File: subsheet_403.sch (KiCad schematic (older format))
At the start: 44 parts, among them Q404 2N3904, Q405 2N3904, U403 MC1377_COLOR_TELEVISION_RGB_T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

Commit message: Delete circuitry related to PAL/NTSC and modulator
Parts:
- removed C415: 470uF, commons_passives_THT:Passive_THT_capacitor_polarized_rad_D10.16mm_P5.08mm_H22.86mm, symbol Device:CP1
- removed C417, C423: 100uF, commons_passives_THT:Passive_THT_capacitor_polarized_rad_D5.08mm_P2.54mm_H12.70mm, symbol Device:CP1
- removed C418: 2200pF, commons_passives_THT:Passive_THT_capacitor_W2.54mm_L10.16mm, symbol Device:C
- removed C419, C422, C428, C429: 0.1uF, commons_passives_THT:Passive_THT_capacitor_mlcc_W2.54mm_L7.62mm, symbol Device:C
- removed C420, C424, C426: 15uF, Capacitor_THT:CP_Radial_Tantal_D4.5mm_P2.50mm, symbol Device:CP1
- removed C421: 120pF, commons_passives_THT:Passive_THT_capacitor_W2.54mm_L10.16mm, symbol Device:C
- removed C425: 2200pF, commons_passives_THT:Passive_THT_capacitor_polarized_rad_D5.08mm_P2.54mm_H12.70mm, symbol Device:C
- removed C427: 0.001uF, commons_passives_THT:Passive_THT_capacitor_W2.54mm_L10.16mm, symbol Device:C
- removed C430, C431: 0.01uF, commons_passives_THT:Passive_THT_capacitor_W2.54mm_L10.16mm, symbol Device:C
- removed C432: 0.001uF, commons_passives_THT:Passive_THT_capacitor_ceramic_radial_W2.54mm_L10.16mm, symbol Device:C
- removed C433: 1uF, commons_passives_THT:Passive_THT_capacitor_polarized_rad_D5.08mm_P2.54mm_H12.70mm, symbol Device:CP1
- removed DL1: Delay Line 3.58MHz, atari-passives_THT:Atari_ST_THT_Delay_Line, symbol Delay_Line_Custom_Atari_ST:Delay_Line_Custom_Atari_ST
- removed L403: Var. coil 24uH, commons_passives_THT:Passive_THT_variable_Coil_Shielded_7x7mm_5_of_6pins, symbol variable_coil_shielded:Variable_Coil_Shielded
- removed MOD1: ST Modulator, Connector_PinHeader_2.54mm:PinHeader_1x03_P2.54mm_Vertical, symbol Connector_Generic_Shielded:Conn_01x03_Shielded
- removed Q404: 2N3904, Package_TO_SOT_THT:TO-92_Inline_Wide, symbol Transistor_BJT:2N3904
- removed R405, R451, R459: 0, commons_passives_THT:Passive_THT_resistor_W2.54mm_L12.70mm, symbol Device:R_Small_US
- removed R439: 75, commons_passives_THT:Passive_THT_resistor_W2.54mm_L12.70mm, symbol Device:R_Small_US
- removed R442, R463, R470: 1K, commons_passives_THT:Passive_THT_resistor_W2.54mm_L12.70mm, symbol Device:R_Small_US
- removed R448: 150, commons_passives_THT:Passive_THT_resistor_W2.54mm_L12.70mm, symbol Device:R_Small_US
- removed R452: 1K5, commons_passives_THT:Passive_THT_resistor_W2.54mm_L12.70mm, symbol Device:R_Small_US
- removed R456: 2K2, commons_passives_THT:Passive_THT_resistor_W2.54mm_L12.70mm, symbol Device:R_Small_US
- removed R467, R468: 1K2, commons_passives_THT:Passive_THT_resistor_W2.54mm_L12.70mm, symbol Device:R_Small_US
- removed R469: 5K6, commons_passives_THT:Passive_THT_resistor_W2.54mm_L12.70mm, symbol Device:R_Small_US
- removed R471: 47K, commons_passives_THT:Passive_THT_resistor_W2.54mm_L12.70mm, symbol Device:R_Small_US
- removed U403: MC1377_COLOR_TELEVISION_RGB_TO_PAL_NTSC_ENCODER_P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, Package_DIP:DIP-20_W7.62mm_LongPads, symbol mc1377:MC1377_COLOR_TELEVISION_RGB_TO_PAL_NTSC_ENCODER_PHY
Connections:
- net labels removed: +12V, AUDIO, B, CCLK, G, NOT__HSYNC_XOR_VSYNC, R, SHIFTER_COLOR, b_y_clamp, blue, chroma_in, chroma_out, cv_out, decoupler, green, ntsc_select, osc_in, r_y_clamp, red, tr, v_clamp, volt_bias, y_in, y_out
- wire segments 130 -> 19
- no-connect marks 6 -> 0
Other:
- note removed: "About L403 and DL1 : I made custom symbols to match the pins written on the schematics.\n\nFor DL1 : \n\nI compared with the schematics of the Atari MegaSTe rev C and of the Falcon030. Pin 12 appears grounded on the former ; on the later, pin 9, 10 and 12 appears grounded, \nwith pin 10 taking the central position, while pin 3 and 6 are bridged together. \n\nIn the gerber of the sparrow (found as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"
- note removed: "C415 should be the other way around. On the ST schematics\nthis is C21, the cathode (-) is connected to the resistor\nthat outputs CSYNC/Composite.\n\nsee https://www.exxoshost.co.uk/forum/viewtopic.php?f=17&t=1698"
- note removed: "Change values for PAL (I took them from the Falcon030 service manual\nafter checking that this part of the schematics is the same as the\nSTe - lucky me)\n\n* C421 : 100pF\n* DL1 : 4.43MHz\n* L403 : 14uH\n* R451 : 22\n* R456 : 1K8 (PAL-I) ; 2K7 (PAL-B)\n* R463 : 1K2\n\nDid you know there was several PAL variant ? \n* PAL-I is for UK/Ireland\n* PAL-B is for Western Europe, Australia and New Zealand"
- note removed: "Installed ONLY in systems with modulator"
- note removed: "NTSC clock"
- note removed: "PAL carrier clock"
- note removed: "Remove\nfor PAL"
- note removed: "bridged on my \nmotherboard"
- note removed: "maybe grounded"

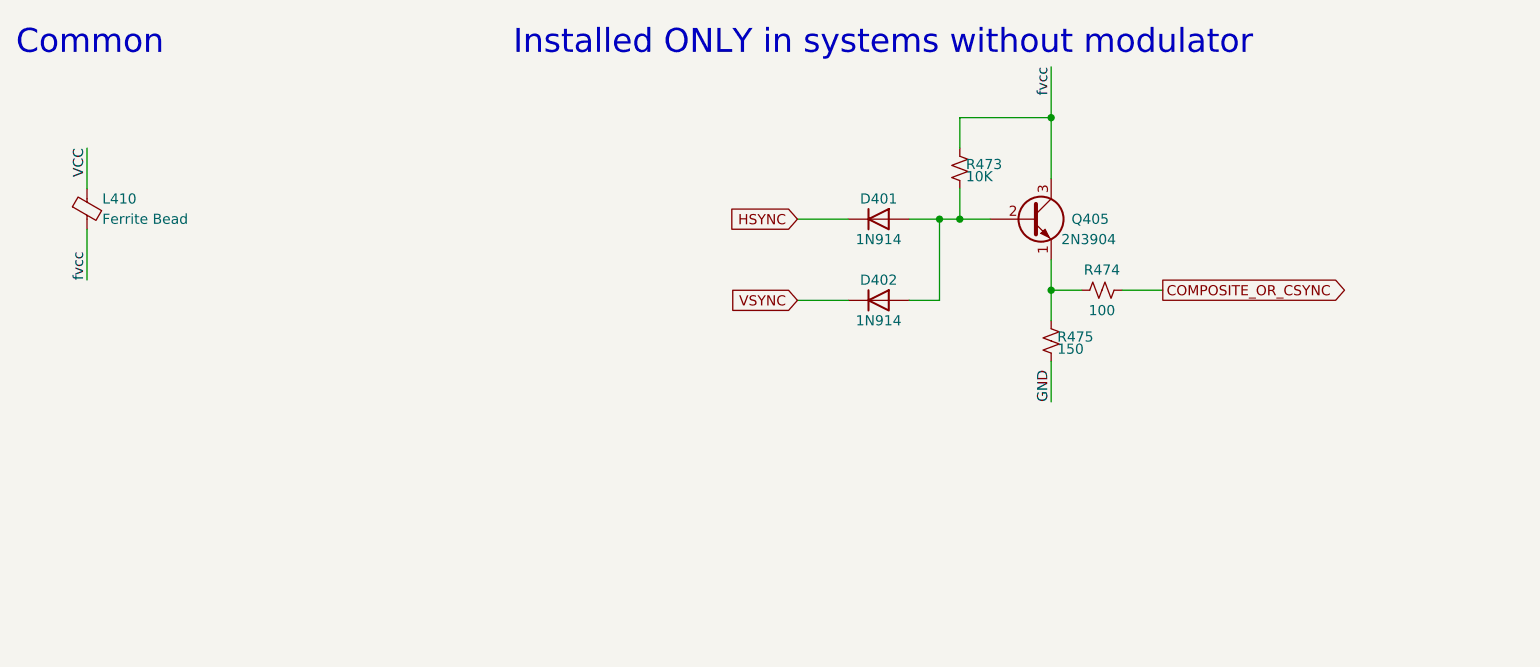
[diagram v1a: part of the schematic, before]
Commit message: Resolves #1 : Use 4-resistor packs wherever it is possible
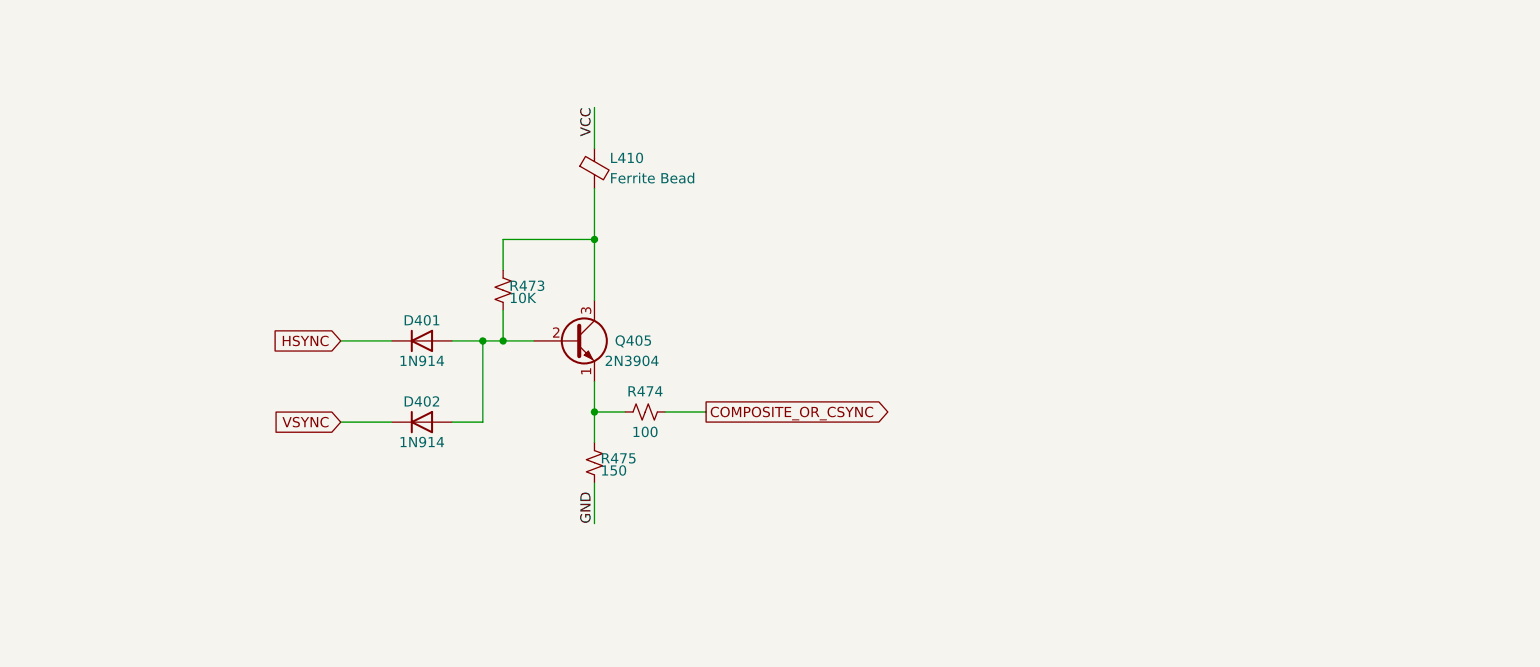
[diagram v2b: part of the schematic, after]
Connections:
- net fvcc: no longer names the net of L410.2, Q405.3 (C), R473.1
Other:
- note removed: "Common"
- note removed: "Installed ONLY in systems without modulator"
- moved on the sheet: D401, D402, L410, Q405, R473, R474, R475
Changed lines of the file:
@@
 L Device:Ferrite_Bead_Small L?
 U 1 1 60C12DAA
-P 1500 1500
+P 4000 1300
 AR Path="/60B3D9E3/60C12DAA" Ref="L?"  Part="1"
 AR Path="/60B8B7AD/60C12DAA" Ref="L410"  Part="1"
-F 0 "L410" H 1575 1550 50  0000 L CNN
-F 1 "Ferrite Bead" H 1575 1450 50  0000 L CNN
-F 2 "commons_passives_THT:Passive_THT_ferrite_bead_W3.81mm_L15.24mm" V 1430 1500 50  0001 C CNN
-F 3 "~" H 1500 1500 50  0001 C CNN
-	1    1500 1500
+F 0 "L410" H 4075 1350 50  0000 L CNN
+F 1 "Ferrite Bead" H 4075 1250 50  0000 L CNN
+F 2 "commons_passives_THT:Passive_THT_ferrite_bead_W3.81mm_L15.24mm" V 3930 1300 50  0001 C CNN
+F 3 "~" H 4000 1300 50  0001 C CNN
+	1    4000 1300
 	1    0    0    -1
 $EndComp
 Wire Wire Line
-	1500 1400 1500 1200
-Text Label 1500 1200 3    50   ~ 0
+	4000 1200 4000 1000
+Text Label 4000 1000 3    50   ~ 0
 VCC
-Text Label 1500 1850 1    50   ~ 0
-fvcc
 Wire Wire Line
-	1500 1850 1500 1600
-Text Notes 3600 750  0    118  ~ 0
-Installed ONLY in systems without modulator
+	4000 1650 4000 1400
 $Comp
 L Transistor_BJT:2N3904 Q?
 U 1 1 60C878BF
-P 6150 1550
+P 3900 2150
 AR Path="/60B3D9E3/60C878BF" Ref="Q?"  Part="1"
 AR Path="/60B8B7AD/60C878BF" Ref="Q405"  Part="1"
-F 0 "Q405" H 6350 1550 50  0000 L CNN
-F 1 "2N3904" H 6300 1450 50  0000 L CNN
-F 2 "Package_TO_SOT_THT:TO-92_Inline_Wide" H 6350 1475 50  0001 L CIN
-F 3 "https://www.onsemi.com/pub/Collateral/2N3903-D.PDF" H 6150 1550 50  0001 L CNN
-	1    6150 1550
+F 0 "Q405" H 4100 2150 50  0000 L CNN
+F 1 "2N3904" H 4050 2050 50  0000 L CNN
+F 2 "Package_TO_SOT_THT:TO-92_Inline_Wide" H 4100 2075 50  0001 L CIN
+F 3 "https://www.onsemi.com/pub/Collateral/2N3903-D.PDF" H 3900 2150 50  0001 L CNN
+	1    3900 2150
 	1    0    0    -1
 $EndComp
@@
 L Device:R_Small_US R?
 U 1 1 60C887E0
-P 5800 1300
+P 3550 1900
 AR Path="/60B3D9E3/60C887E0" Ref="R?"  Part="1"
 AR Path="/60B8B7AD/60C887E0" Ref="R473"  Part="1"
-F 0 "R473" H 5830 1320 50  0000 L CNN
-F 1 "10K" H 5830 1260 50  0000 L CNN
-F 2 "commons_passives_THT:Passive_THT_resistor_W2.54mm_L12.70mm" H 5800 1300 50  0001 C CNN
-F 3 "~" H 5800 1300 50  0001 C CNN
-	1    5800 1300
+F 0 "R473" H 3580 1920 50  0000 L CNN
+F 1 "10K" H 3580 1860 50  0000 L CNN
+F 2 "commons_passives_THT:Passive_THT_resistor_W2.54mm_L12.70mm" H 3550 1900 50  0001 C CNN
+F 3 "~" H 3550 1900 50  0001 C CNN
+	1    3550 1900
 	1    0    0    -1
 $EndComp
@@
 L Device:R_Small_US R?
 U 1 1 60C8E2E8
-P 6250 2150
+P 4000 2750
 AR Path="/60B3D9E3/60C8E2E8" Ref="R?"  Part="1"
 AR Path="/60B8B7AD/60C8E2E8" Ref="R475"  Part="1"
-F 0 "R475" H 6280 2170 50  0000 L CNN
-F 1 "150" H 6280 2110 50  0000 L CNN
-F 2 "commons_passives_THT:Passive_THT_resistor_W2.54mm_L12.70mm" H 6250 2150 50  0001 C CNN
-F 3 "~" H 6250 2150 50  0001 C CNN
-	1    6250 2150
+F 0 "R475" H 4030 2770 50  0000 L CNN
+F 1 "150" H 4030 2710 50  0000 L CNN
+F 2 "commons_passives_THT:Passive_THT_resistor_W2.54mm_L12.70mm" H 4000 2750 50  0001 C CNN
+F 3 "~" H 4000 2750 50  0001 C CNN
+	1    4000 2750
 	1    0    0    -1
 $EndComp
-Text Label 6250 2450 1    50   ~ 0
+Text Label 4000 3050 1    50   ~ 0
 GND
 Wire Wire Line
-	6250 2250 6250 2450
+	4000 2850 4000 3050
 $Comp
 L Device:R_Small_US R?
 U 1 1 60C9CC6E
-P 6500 1900
+P 4250 2500
 AR Path="/608A2359/60C9CC6E" Ref="R?"  Part="1"
 AR Path="/60A1445F/60C9CC6E" Ref="R?"  Part="1"
@@
 AR Path="/60B3D9E3/60C9CC6E" Ref="R?"  Part="1"
 AR Path="/60B8B7AD/60C9CC6E" Ref="R474"  Part="1"
-F 0 "R474" V 6400 1900 50  0000 C CNN
-F 1 "100" V 6600 1900 50  0000 C CNN
-F 2 "commons_passives_THT:Passive_THT_resistor_W2.54mm_L12.70mm" H 6500 1900 50  0001 C CNN
-F 3 "~" H 6500 1900 50  0001 C CNN
-	1    6500 1900
+F 0 "R474" V 4150 2500 50  0000 C CNN
+F 1 "100" V 4350 2500 50  0000 C CNN
+F 2 "commons_passives_THT:Passive_THT_resistor_W2.54mm_L12.70mm" H 4250 2500 50  0001 C CNN
+F 3 "~" H 4250 2500 50  0001 C CNN
+	1    4250 2500
 	0    1    1    0
 $EndComp
@@
 L Device:D D401
 U 1 1 60CA07DA
-P 5400 1550
-F 0 "D401" H 5400 1650 50  0000 C CNN
-F 1 "1N914" H 5400 1450 50  0000 C CNN
-F 2 "commons_passives_THT:Passive_THT_diode_W2.54mm_L12.70mm" H 5400 1550 50  0001 C CNN
-F 3 "~" H 5400 1550 50  0001 C CNN
-	1    5400 1550
+P 3150 2150
+F 0 "D401" H 3150 2250 50  0000 C CNN
+F 1 "1N914" H 3150 2050 50  0000 C CNN
+F 2 "commons_passives_THT:Passive_THT_diode_W2.54mm_L12.70mm" H 3150 2150 50  0001 C CNN
+F 3 "~" H 3150 2150 50  0001 C CNN
+	1    3150 2150
 	1    0    0    -1
 $EndComp
@@
 L Device:D D402
 U 1 1 60CA1114
-P 5400 1950
-F 0 "D402" H 5400 2050 50  0000 C CNN
-F 1 "1N914" H 5400 1850 50  0000 C CNN
-F 2 "commons_passives_THT:Passive_THT_diode_W2.54mm_L12.70mm" H 5400 1950 50  0001 C CNN
-F 3 "~" H 5400 1950 50  0001 C CNN
-	1    5400 1950
+P 3150 2550
+F 0 "D402" H 3150 2650 50  0000 C CNN
+F 1 "1N914" H 3150 2450 50  0000 C CNN
+F 2 "commons_passives_THT:Passive_THT_diode_W2.54mm_L12.70mm" H 3150 2550 50  0001 C CNN
+F 3 "~" H 3150 2550 50  0001 C CNN
+	1    3150 2550
 	1    0    0    -1
 $EndComp
-Text Label 6250 800  3    50   ~ 0
-fvcc
 Wire Wire Line
-	6250 800  6250 1050
+	4000 1650 3550 1650
 Wire Wire Line
-	6250 1050 5800 1050
+	3550 1650 3550 1800
+Connection ~ 4000 1650
 Wire Wire Line
-	5800 1050 5800 1200
-Connection ~ 6250 1050
+	4000 1650 4000 1950
 Wire Wire Line
-	6250 1050 6250 1350
+	3550 2000 3550 2150
 Wire Wire Line
-	5800 1400 5800 1550
+	3550 2150 3700 2150
 Wire Wire Line
-	5800 1550 5950 1550
+	3300 2150 3450 2150
+Connection ~ 3550 2150
 Wire Wire Line
-	5550 1550 5700 1550
-Connection ~ 5800 1550
+	3300 2550 3450 2550
 Wire Wire Line
-	5550 1950 5700 1950
+	3450 2550 3450 2150
+Connection ~ 3450 2150
 Wire Wire Line
-	5700 1950 5700 1550
-Connection ~ 5700 1550
+	3450 2150 3550 2150
 Wire Wire Line
-	5700 1550 5800 1550
+	4000 2350 4000 2500
 Wire Wire Line
-	6250 1750 6250 1900
+	4000 2500 4150 2500
+Connection ~ 4000 2500
 Wire Wire Line
-	6250 1900 6400 1900
-Connection ~ 6250 1900
-Wire Wire Line
-	6250 1900 6250 2050
-Text GLabel 6800 1900 2    50   Output ~ 0
+	4000 2500 4000 2650
+Text GLabel 4550 2500 2    50   Output ~ 0
 COMPOSITE_OR_CSYNC
 Wire Wire Line
-	6600 1900 6800 1900
-Text GLabel 5000 1550 0    50   Input ~ 0
+	4350 2500 4550 2500
+Text GLabel 2750 2150 0    50   Input ~ 0
 HSYNC
-Text GLabel 5000 1950 0    50   Input ~ 0
+Text GLabel 2750 2550 0    50   Input ~ 0
 VSYNC
 Wire Wire Line
-	5000 1550 5250 1550
+	2750 2150 3000 2150
 Wire Wire Line
-	5000 1950 5250 1950
-Text Notes 1150 750  0    118  ~ 0
-Common
+	2750 2550 3000 2550
 Wire Notes Line
 	7800 5900 7800 5400

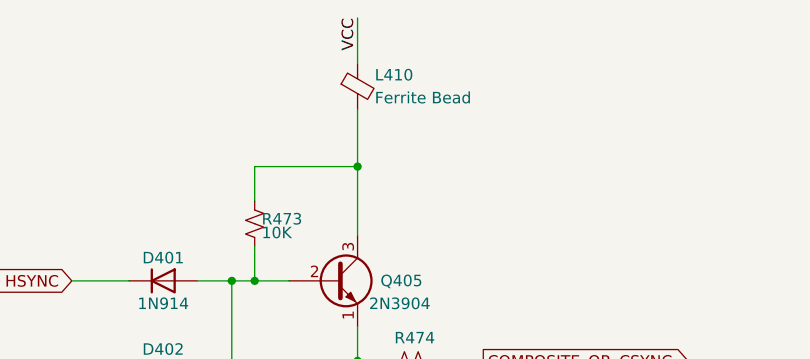
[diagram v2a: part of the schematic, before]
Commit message: Resolves #11 : Use the reference 'FB?' for the ferrite beads
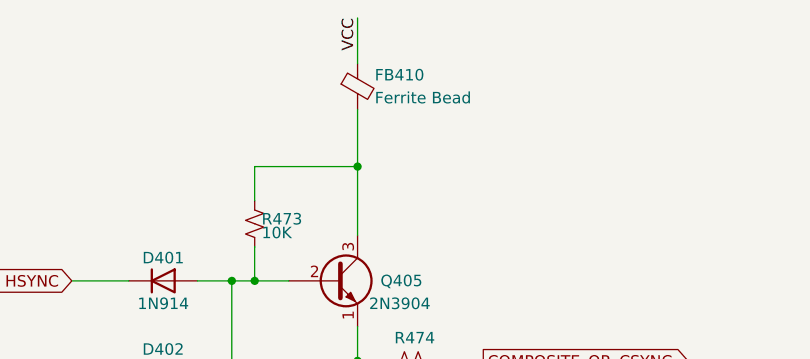
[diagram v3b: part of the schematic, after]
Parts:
- renumbered L410 to FB410
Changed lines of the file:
@@
 P 4000 1300
 AR Path="/60B3D9E3/60C12DAA" Ref="L?"  Part="1"
-AR Path="/60B8B7AD/60C12DAA" Ref="L410"  Part="1"
-F 0 "L410" H 4075 1350 50  0000 L CNN
+AR Path="/60B8B7AD/60C12DAA" Ref="FB410"  Part="1"
+F 0 "FB410" H 4075 1350 50  0000 L CNN
 F 1 "Ferrite Bead" H 4075 1250 50  0000 L CNN
 F 2 "commons_passives_THT:Passive_THT_ferrite_bead_W3.81mm_L15.24mm" V 3930 1300 50  0001 C CNN

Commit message: Resolves #13 : assign 1206 hand-solder footprints to resistors
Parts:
- R473, R474, R475: footprint commons_passives_THT:Passive_THT_resistor_W2.54mm_L12.70mm -> Resistor_SMD:R_1206_3216Metric_Pad1.30x1.75mm_HandSolder
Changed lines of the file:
@@
 F 0 "R473" H 3580 1920 50  0000 L CNN
 F 1 "10K" H 3580 1860 50  0000 L CNN
-F 2 "commons_passives_THT:Passive_THT_resistor_W2.54mm_L12.70mm" H 3550 1900 50  0001 C CNN
+F 2 "Resistor_SMD:R_1206_3216Metric_Pad1.30x1.75mm_HandSolder" H 3550 1900 50  0001 C CNN
 F 3 "~" H 3550 1900 50  0001 C CNN
 	1    3550 1900
@@
 F 0 "R475" H 4030 2770 50  0000 L CNN
 F 1 "150" H 4030 2710 50  0000 L CNN
-F 2 "commons_passives_THT:Passive_THT_resistor_W2.54mm_L12.70mm" H 4000 2750 50  0001 C CNN
+F 2 "Resistor_SMD:R_1206_3216Metric_Pad1.30x1.75mm_HandSolder" H 4000 2750 50  0001 C CNN
 F 3 "~" H 4000 2750 50  0001 C CNN
 	1    4000 2750
@@
 F 0 "R474" V 4150 2500 50  0000 C CNN
 F 1 "100" V 4350 2500 50  0000 C CNN
-F 2 "commons_passives_THT:Passive_THT_resistor_W2.54mm_L12.70mm" H 4250 2500 50  0001 C CNN
+F 2 "Resistor_SMD:R_1206_3216Metric_Pad1.30x1.75mm_HandSolder" H 4250 2500 50  0001 C CNN
 F 3 "~" H 4250 2500 50  0001 C CNN
 	1    4250 2500

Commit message: Resolves #14 : assign smd footprints for ferrite beads
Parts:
- FB410: footprint commons_passives_THT:Passive_THT_ferrite_bead_W3.81mm_L15.24mm -> Inductor_SMD:L_1206_3216Metric_Pad1.22x1.90mm_HandSolder
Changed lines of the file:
@@
 F 0 "FB410" H 4075 1350 50  0000 L CNN
 F 1 "Ferrite Bead" H 4075 1250 50  0000 L CNN
-F 2 "commons_passives_THT:Passive_THT_ferrite_bead_W3.81mm_L15.24mm" V 3930 1300 50  0001 C CNN
+F 2 "Inductor_SMD:L_1206_3216Metric_Pad1.22x1.90mm_HandSolder" V 3930 1300 50  0001 C CNN
 F 3 "~" H 4000 1300 50  0001 C CNN
 	1    4000 1300

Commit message: Resolves #16 : assign smd footprints to diodes
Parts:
- D401, D402: footprint commons_passives_THT:Passive_THT_diode_W2.54mm_L12.70mm -> Diode_SMD:D_SOD-123F
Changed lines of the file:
@@
 F 0 "D401" H 3150 2250 50  0000 C CNN
 F 1 "1N914" H 3150 2050 50  0000 C CNN
-F 2 "commons_passives_THT:Passive_THT_diode_W2.54mm_L12.70mm" H 3150 2150 50  0001 C CNN
+F 2 "Diode_SMD:D_SOD-123F" H 3150 2150 50  0001 C CNN
 F 3 "~" H 3150 2150 50  0001 C CNN
 	1    3150 2150
@@
 F 0 "D402" H 3150 2650 50  0000 C CNN
 F 1 "1N914" H 3150 2450 50  0000 C CNN
-F 2 "commons_passives_THT:Passive_THT_diode_W2.54mm_L12.70mm" H 3150 2550 50  0001 C CNN
+F 2 "Diode_SMD:D_SOD-123F" H 3150 2550 50  0001 C CNN
 F 3 "~" H 3150 2550 50  0001 C CNN
 	1    3150 2550

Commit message: Resolves #17 : assign smd footprints to transistors
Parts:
- Q405: footprint Package_TO_SOT_THT:TO-92_Inline_Wide -> Package_TO_SOT_SMD:SOT-23
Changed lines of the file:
@@
 F 0 "Q405" H 4100 2150 50  0000 L CNN
 F 1 "2N3904" H 4050 2050 50  0000 L CNN
-F 2 "Package_TO_SOT_THT:TO-92_Inline_Wide" H 4100 2075 50  0001 L CIN
+F 2 "Package_TO_SOT_SMD:SOT-23" H 4100 2075 50  0001 L CIN
 F 3 "https://www.onsemi.com/pub/Collateral/2N3903-D.PDF" H 3900 2150 50  0001 L CNN
 	1    3900 2150
